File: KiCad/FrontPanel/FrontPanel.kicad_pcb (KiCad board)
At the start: 2 copper layers, 83 x 29 mm, 13 parts, among them J1 5V, J2 GND

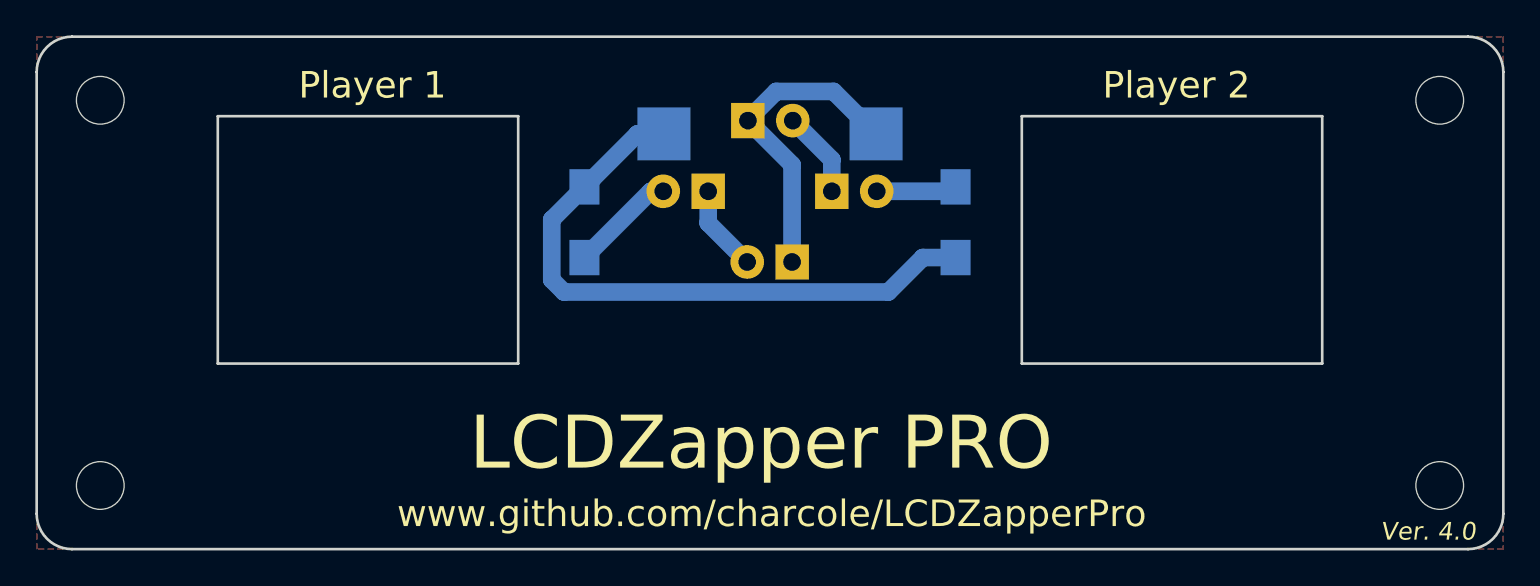
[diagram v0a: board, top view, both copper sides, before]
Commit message: Expose ground through screws
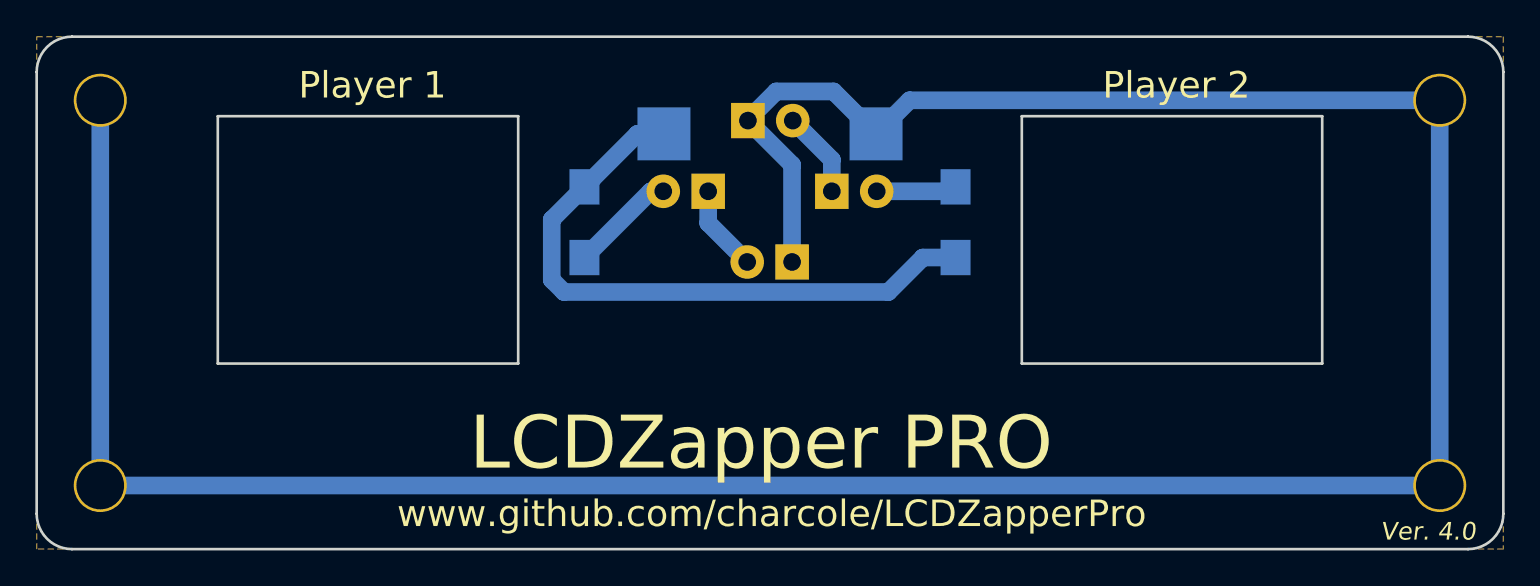
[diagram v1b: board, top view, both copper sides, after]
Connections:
- REF** pad 1: (no net) -> GND (x4)
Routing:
- net GND: track 18.0 -> 170.1 mm
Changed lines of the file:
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@@
 (kicad_pcb (version 4) (host pcbnew 4.0.6)
   (general
-    (links 8)
+    (links 12)
     (no_connects 0)
-    (area 99.924999 69.924999 183.075001 99.075001)
+    (area 93.328572 68.925 204.235715 119.944961)
     (thickness 1.6)
     (drawings 30)
-    (tracks 25)
+    (tracks 30)
     (zones 0)
     (modules 13)
@@
     (mod_text_size 1 1)
     (mod_text_width 0.15)
-    (pad_size 18 1.8)
-    (pad_drill 18)
+    (pad_size 3 3)
+    (pad_drill 2.7)
     (pad_to_mask_clearance 0.2)
     (aux_axis_origin 0 0)
@@
     (fp_circle (center 0 0) (end 2.7 0) (layer Cmts.User) (width 0.15))
     (fp_circle (center 0 0) (end 2.95 0) (layer F.CrtYd) (width 0.05))
-    (pad 1 np_thru_hole circle (at 0 0) (size 2.7 2.7) (drill 2.7) (layers *.Cu *.Mask))
+    (pad 1 thru_hole circle (at 0 0) (size 3 3) (drill 2.7) (layers *.Cu *.Mask)
+      (net 3 GND))
   )
   (module Mounting_Holes:MountingHole_2.7mm_M2.5 (layer F.Cu)
@@
     (fp_circle (center 0 0) (end 2.7 0) (layer Cmts.User) (width 0.15))
     (fp_circle (center 0 0) (end 2.95 0) (layer F.CrtYd) (width 0.05))
-    (pad 1 np_thru_hole circle (at 0 0) (size 2.7 2.7) (drill 2.7) (layers *.Cu *.Mask))
+    (pad 1 thru_hole circle (at 0 0) (size 3 3) (drill 2.7) (layers *.Cu *.Mask)
+      (net 3 GND))
   )
   (module Mounting_Holes:MountingHole_2.7mm_M2.5 (layer F.Cu)
@@
     (fp_circle (center 0 0) (end 2.7 0) (layer Cmts.User) (width 0.15))
     (fp_circle (center 0 0) (end 2.95 0) (layer F.CrtYd) (width 0.05))
-    (pad 1 np_thru_hole circle (at 0 0) (size 2.7 2.7) (drill 2.7) (layers *.Cu *.Mask))
+    (pad 1 thru_hole circle (at 0 0) (size 3 3) (drill 2.7) (layers *.Cu *.Mask)
+      (net 3 GND))
   )
   (module Mounting_Holes:MountingHole_2.7mm_M2.5 (layer F.Cu)
@@
     (fp_circle (center 0 0) (end 2.7 0) (layer Cmts.User) (width 0.15))
     (fp_circle (center 0 0) (end 2.95 0) (layer F.CrtYd) (width 0.05))
-    (pad 1 np_thru_hole circle (at 0 0) (size 2.7 2.7) (drill 2.7) (layers *.Cu *.Mask))
+    (pad 1 thru_hole circle (at 0 0) (size 3 3) (drill 2.7) (layers *.Cu *.Mask)
+      (net 3 GND))
   )
   (module Mounting_Holes:MountingHole_2.7mm_M2.5 (layer F.Cu)
@@
   (segment (start 151.75 78.75) (end 152 78.5) (width 1) (layer B.Cu) (net 2))
   (segment (start 151.75 78.25) (end 152 78.5) (width 1) (layer B.Cu) (net 2))
+  (segment (start 179.4 73.6) (end 149.4 73.6) (width 1) (layer B.Cu) (net 3))
+  (segment (start 149.4 73.6) (end 147.5 75.5) (width 1) (layer B.Cu) (net 3))
+  (segment (start 179.4 95.4) (end 179.4 73.6) (width 1) (layer B.Cu) (net 3))
+  (segment (start 103.6 95.4) (end 179.4 95.4) (width 1) (layer B.Cu) (net 3))
+  (segment (start 103.6 73.6) (end 103.6 95.4) (width 1) (layer B.Cu) (net 3))
   (segment (start 140.25 74.75) (end 140.25 74.7) (width 1) (layer B.Cu) (net 3))
   (segment (start 141.850001 73.099999) (end 145.099999 73.099999) (width 1) (layer B.Cu) (net 3))
